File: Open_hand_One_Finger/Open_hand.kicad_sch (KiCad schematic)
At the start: 10 parts, among them U2 MAX32660GTP

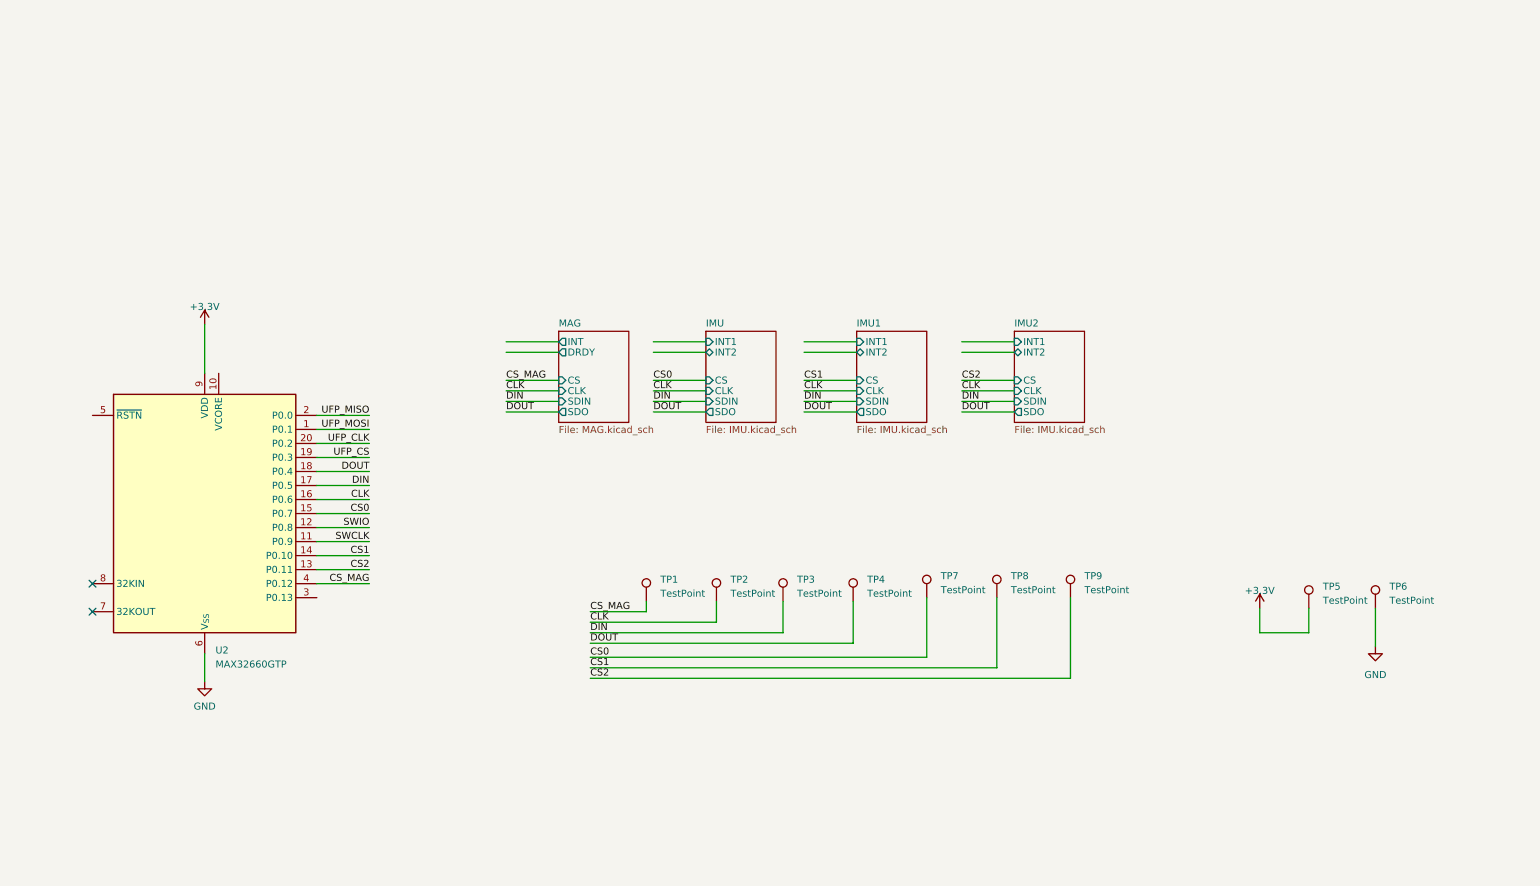
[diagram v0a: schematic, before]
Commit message: add swd conector
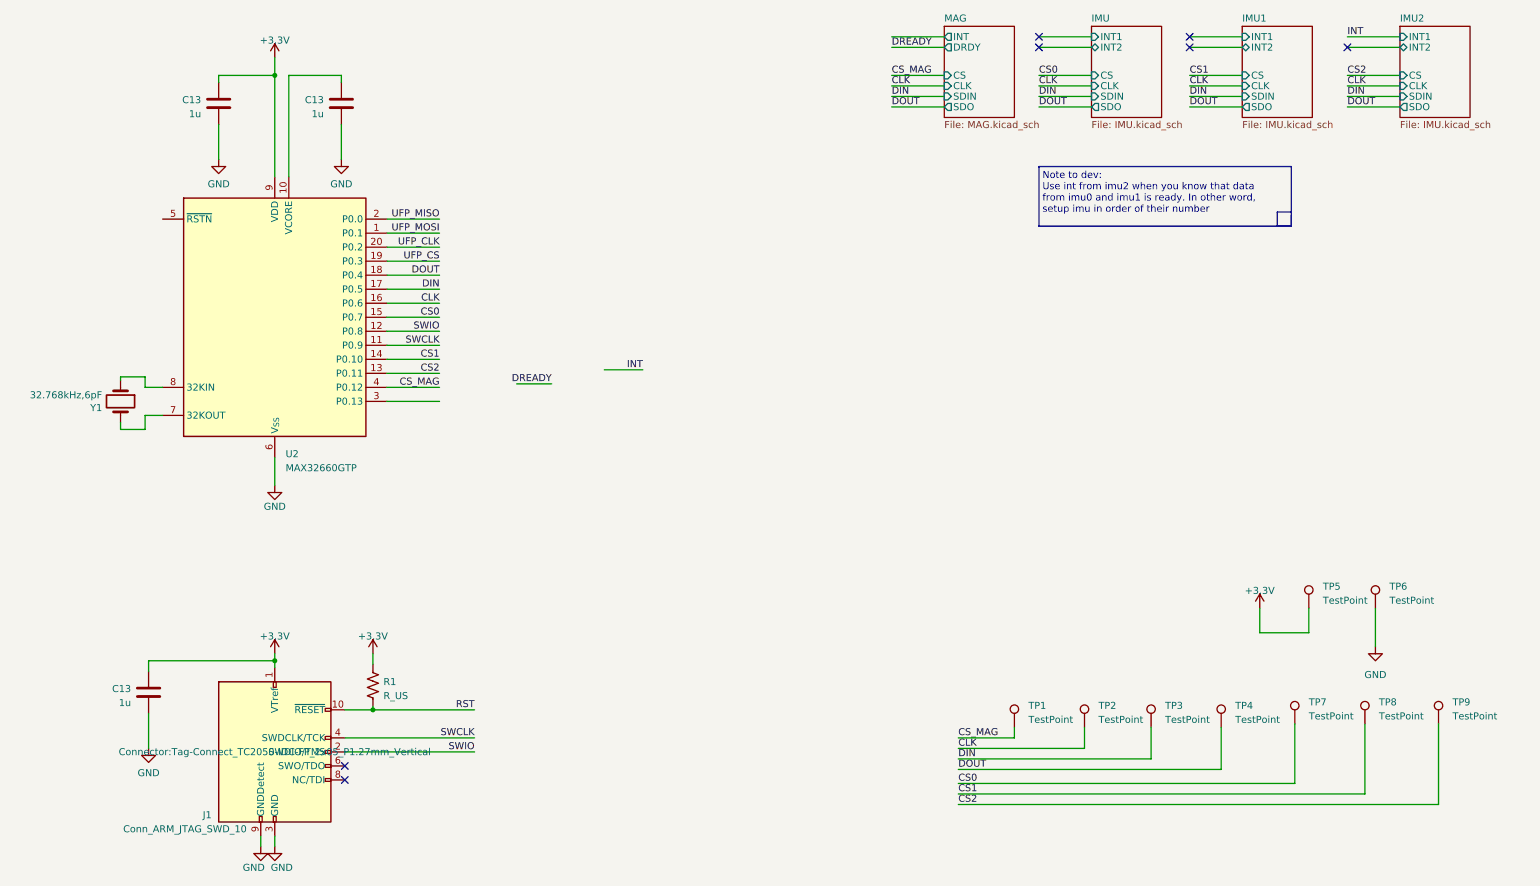
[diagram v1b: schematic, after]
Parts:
- added C13 (x3): 1u, Capacitor_SMD:C_0603_1608Metric, symbol Device:C
- added J1: Conn_ARM_JTAG_SWD_10, Connector:Tag-Connect_TC2050-IDC-FP_2x05_P1.27mm_Vertical, symbol Connector:Conn_ARM_JTAG_SWD_10
- added R1: R_US, symbol Device:R_US
- added Y1: 32.768kHz,6pF, Crystal:Crystal_SMD_3215-2Pin_3.2x1.5mm, symbol Device:Crystal
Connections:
- net +3.3V: now also C13.1, C13.1, J1.1 (VTref), R1.1
- net GND: now also C13.2, C13.2, C13.2, J1.3 (GND), J1.5 (GND), J1.9 (GNDDetect)
- net SWCLK: now also J1.4 (SWDCLK/TCK)
- net SWIO: now also J1.2 (SWDIO/TMS)
- net at U2.10 (VCORE): now also C13.1
- net at U2.7 (32KOUT): now also Y1.2
- net at U2.8 (32KIN): now also Y1.1
- new net RST: J1.10 (~{RESET}), R1.2
- no-connect marks 2 -> 7
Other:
- note added: "Note to dev: Use int from imu2 when you know that data from imu0 and imu1 is ready. In other word, setup imu in order of their number"
- moved on the sheet: TP1, TP2, TP3, TP4, TP7, TP8, TP9, U2
